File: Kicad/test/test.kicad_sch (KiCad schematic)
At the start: 72 parts, among them J1 SPKOUT, J2 PrgmUART, P1 USB_C_Plug_USB2.0, SW1 SW_Push, SW2 SW_Push, SW3 SW_Push, SW4 SW_Push, SW5 SW_Push, U1 MAX98357A, U2 ESP32-S3-WROOM-1

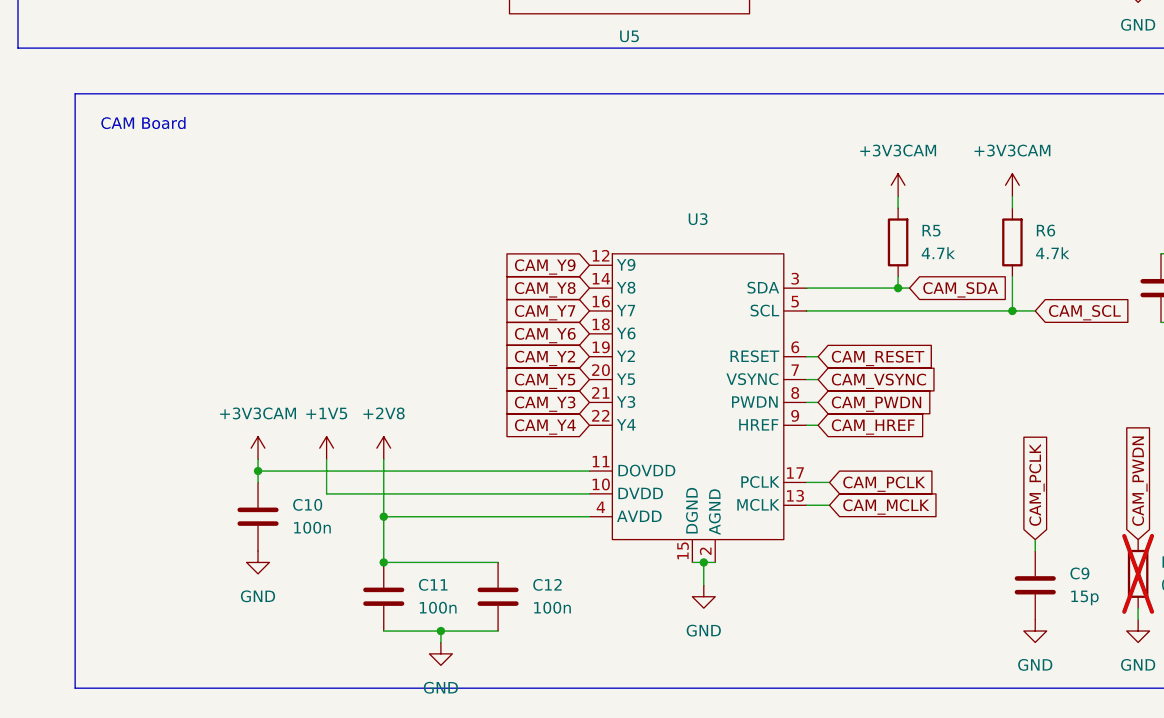
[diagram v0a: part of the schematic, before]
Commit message: Added Clock for Camera
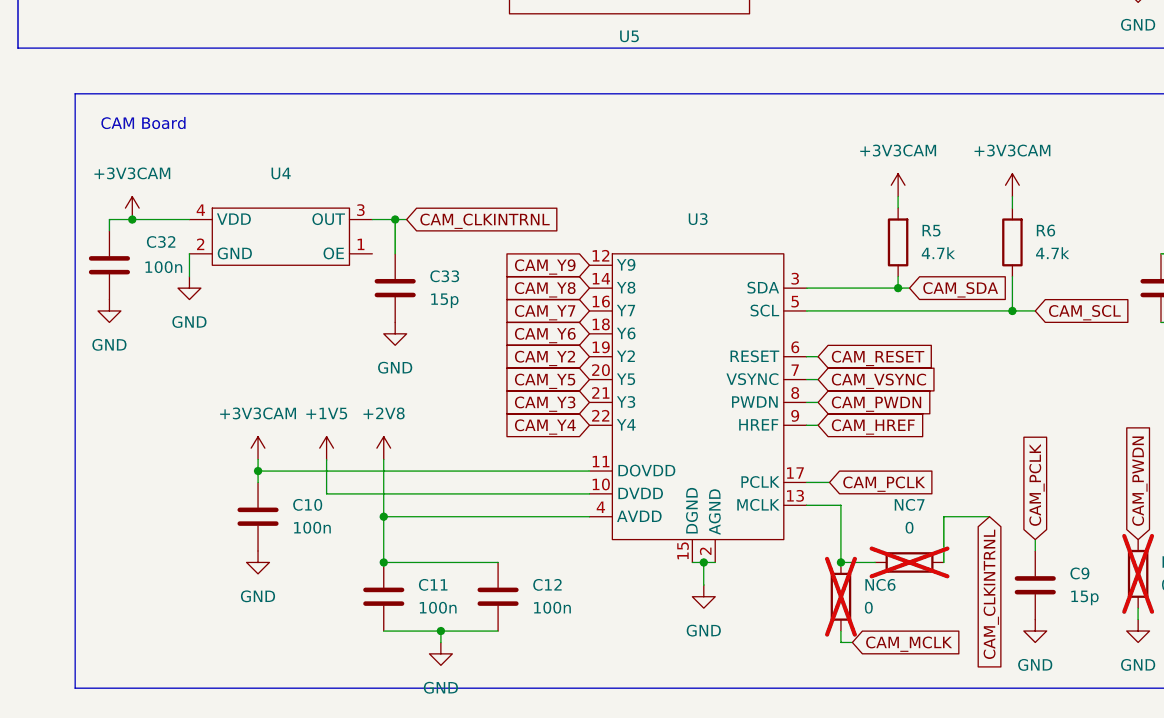
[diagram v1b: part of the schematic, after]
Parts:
- added C32: 100n, Capacitor_SMD:C_0603_1608Metric_Pad1.08x0.95mm_HandSolder, symbol Device:C
- added C33: 15p, Capacitor_SMD:C_0603_1608Metric_Pad1.08x0.95mm_HandSolder, symbol Device:C
- added NC6, NC7: 0, Resistor_SMD:R_1206_3216Metric, symbol Device:R
- added U4: ~, Footprint_Wareit_Mic:YSO110TR, symbol Components_Wareit_Mic:YSO110TR
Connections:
- net +3V3CAM: now also C32.1, U4.4 (VDD)
- net CAM_MCLK: now also NC6.2; no longer U3.13 (MCLK)
- net GND: now also C32.2, C33.2, U4.2 (GND)
- new net: NC6.1, NC7.2, U3.13 (MCLK)
- new net CAM_CLKINTRNL: C33.1, NC7.1, U4.3 (OUT)

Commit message: 3d Model Casing and PCB Added
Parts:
- removed D2: WS2812B, LED_SMD:LED_WS2812B_PLCC4_5.0x5.0mm_P3.2mm, symbol LED:WS2812B
- D4: LCSC Part (none) -> C22461793; Mfr Part (none) -> XL-5050RGBC-WS2812B-S
- L1, L2: footprint Capacitor_SMD:C_0603_1608Metric_Pad1.08x0.95mm_HandSolder -> Inductor_SMD:L_0805_2012Metric_Pad1.05x1.20mm_HandSolder; LCSC Part (none) -> C6364721; Mfr Part (none) -> AHW2012F-1R0KTF
- MK2: LCSC Part (none) -> C5656610; Mfr Part (none) -> ICS-43434
- P1: LCSC Part (none) -> C223907; Mfr Part (none) -> TYPE-C-31-M-14
- SW2, SW3, SW4: LCSC Part (none) -> C136662; Mfr Part (none) -> K2-1114SA-A4SW-06
- SW5: LCSC Part (none) -> C2733655; Mfr Part (none) -> B3S-1000
- U1: LCSC Part (none) -> C2682619; Mfr Part (none) -> MAX98357AEWL+T
- U3: value ~ -> OV5640; LCSC Part (none) -> C262669; Mfr Part (none) -> AFC01-S24FCA-00
- U4: value ~ -> 24Mhz; LCSC Part (none) -> C669072; Mfr Part (none) -> OT252024MJBA4SL
- U5: value ~ -> AXP2101; LCSC Part (none) -> C3036461; Mfr Part (none) -> AXP2101
- renumbered 3v3J to 3v3J1

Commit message: Floorplanning done
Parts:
- removed SW1: SW_Push, Button_Switch_SMD:SW_SPST_B3S-1000, symbol Switch:SW_Push
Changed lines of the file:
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@@
 	(wire
 		(pts
-			(xy 278.13 198.12) (xy 276.86 198.12)
-		)
-		(stroke
-			(width 0)
-			(type default)
-		)
-	)
-	(wire
-		(pts
 			(xy 214.63 96.52) (xy 222.25 96.52)
 		)
@@
 	(wire
 		(pts
-			(xy 276.86 198.12) (xy 276.86 201.93)
-		)
-		(stroke
-			(width 0)
-			(type default)
-		)
-	)
-	(wire
-		(pts
 			(xy 154.94 172.72) (xy 154.94 171.45)
 		)
@@
 		)
 	)
-	(global_label "EN"
-		(shape input)
-		(at 288.29 198.12 0)
-		(fields_autoplaced yes)
-		(effects
-			(font
-				(size 1.27 1.27)
-			)
-			(justify left)
-		)
-		(property "Intersheetrefs" "${INTERSHEET_REFS}"
-			(at 293.7547 198.12 0)
-			(effects
-				(font
-					(size 1.27 1.27)
-				)
-				(justify left)
-				(hide yes)
-			)
-		)
-	)
 	(global_label "CAM_MCLK"
 		(shape input)
@@
 	)
 	(symbol
-		(lib_id "power:GND")
-		(at 276.86 201.93 0)
-		(unit 1)
-		(exclude_from_sim no)
-		(in_bom yes)
-		(on_board yes)
-		(dnp no)
-		(property "Reference" "#PWR027"
-			(at 276.86 208.28 0)
-			(effects
-				(font
-					(size 1.27 1.27)
-				)
-				(hide yes)
-			)
-		)
-		(property "Value" "GND"
-			(at 276.86 207.01 0)
-			(effects
-				(font
-					(size 1.27 1.27)
-				)
-			)
-		)
-		(property "Footprint" ""
-			(at 276.86 201.93 0)
-			(effects
-				(font
-					(size 1.27 1.27)
-				)
-				(hide yes)
-			)
-		)
-		(property "Datasheet" ""
-			(at 276.86 201.93 0)
-			(effects
-				(font
-					(size 1.27 1.27)
-				)
-				(hide yes)
-			)
-		)
-		(property "Description" "Power symbol creates a global label with name \"GND\" , ground"
-			(at 276.86 201.93 0)
-			(effects
-				(font
-					(size 1.27 1.27)
-				)
-				(hide yes)
-			)
-		)
-		(pin "1"
-		)
-		(instances
-			(project "test"
-				(path "/2b9d0de6-8b12-4765-99af-867ac9f145de"
-					(reference "#PWR027")
-					(unit 1)
-				)
-			)
-		)
-	)
-	(symbol
 		(lib_id "Device:C")
 		(at 198.12 133.35 180)
@@
 					(unit 1)
 				)
-			)
-		)
-	)
-	(symbol
-		(lib_id "Switch:SW_Push")
-		(at 283.21 198.12 0)
-		(unit 1)
-		(exclude_from_sim no)
-		(in_bom yes)
-		(on_board yes)
-		(dnp no)
-		(fields_autoplaced yes)
-		(property "Reference" "SW1"
-			(at 283.21 190.5 0)
-			(effects
-				(font
-					(size 1.27 1.27)
-				)
-			)
-		)
-		(property "Value" "SW_Push"
-			(at 283.21 193.04 0)
-			(effects
-				(font
-					(size 1.27 1.27)
-				)
-			)
-		)
-		(property "Footprint" "Button_Switch_SMD:SW_SPST_B3S-1000"
-			(at 283.21 193.04 0)
-			(effects
-				(font
-					(size 1.27 1.27)
-				)
-				(hide yes)
-			)
-		)
-		(property "Datasheet" "~"
-			(at 283.21 193.04 0)
-			(effects
-				(font
-					(size 1.27 1.27)
-				)
-				(hide yes)
-			)
-		)
-		(property "Description" "Push button switch, generic, two pins"
-			(at 283.21 198.12 0)
-			(effects
-				(font
-					(size 1.27 1.27)
-				)
-				(hide yes)
-			)
-		)
-		(pin "1"
-		)
-		(pin "2"
-		)
-		(instances
-			(project ""
-				(path "/2b9d0de6-8b12-4765-99af-867ac9f145de"
-					(reference "SW1")
-					(unit 1)
-				)

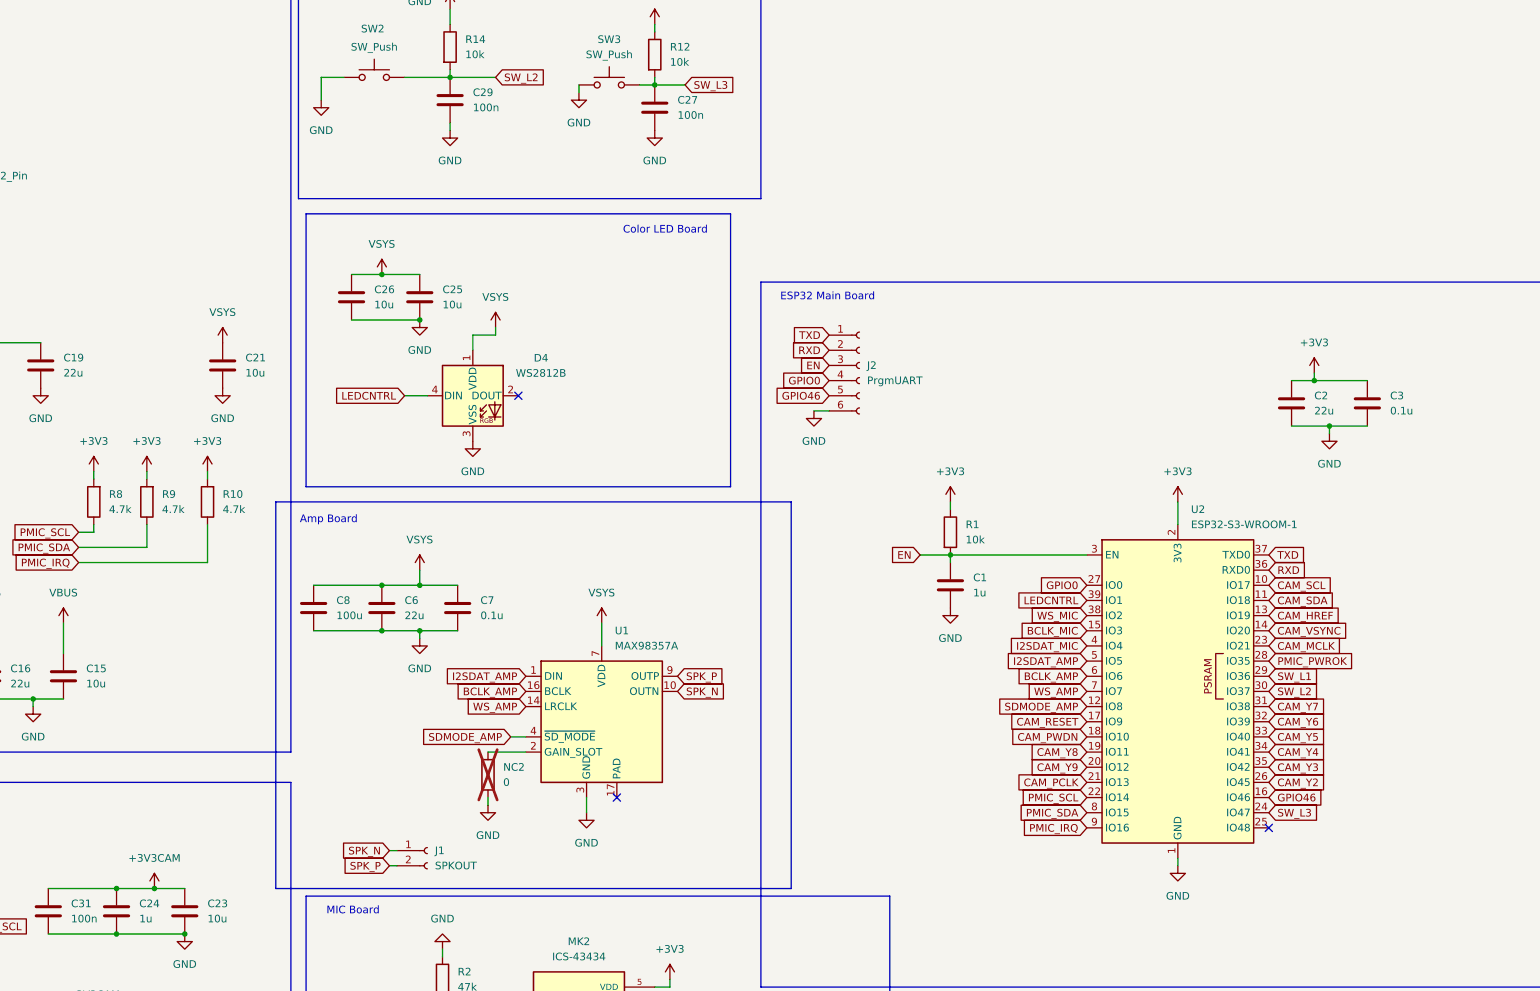
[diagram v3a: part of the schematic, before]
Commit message: Started PCB routing
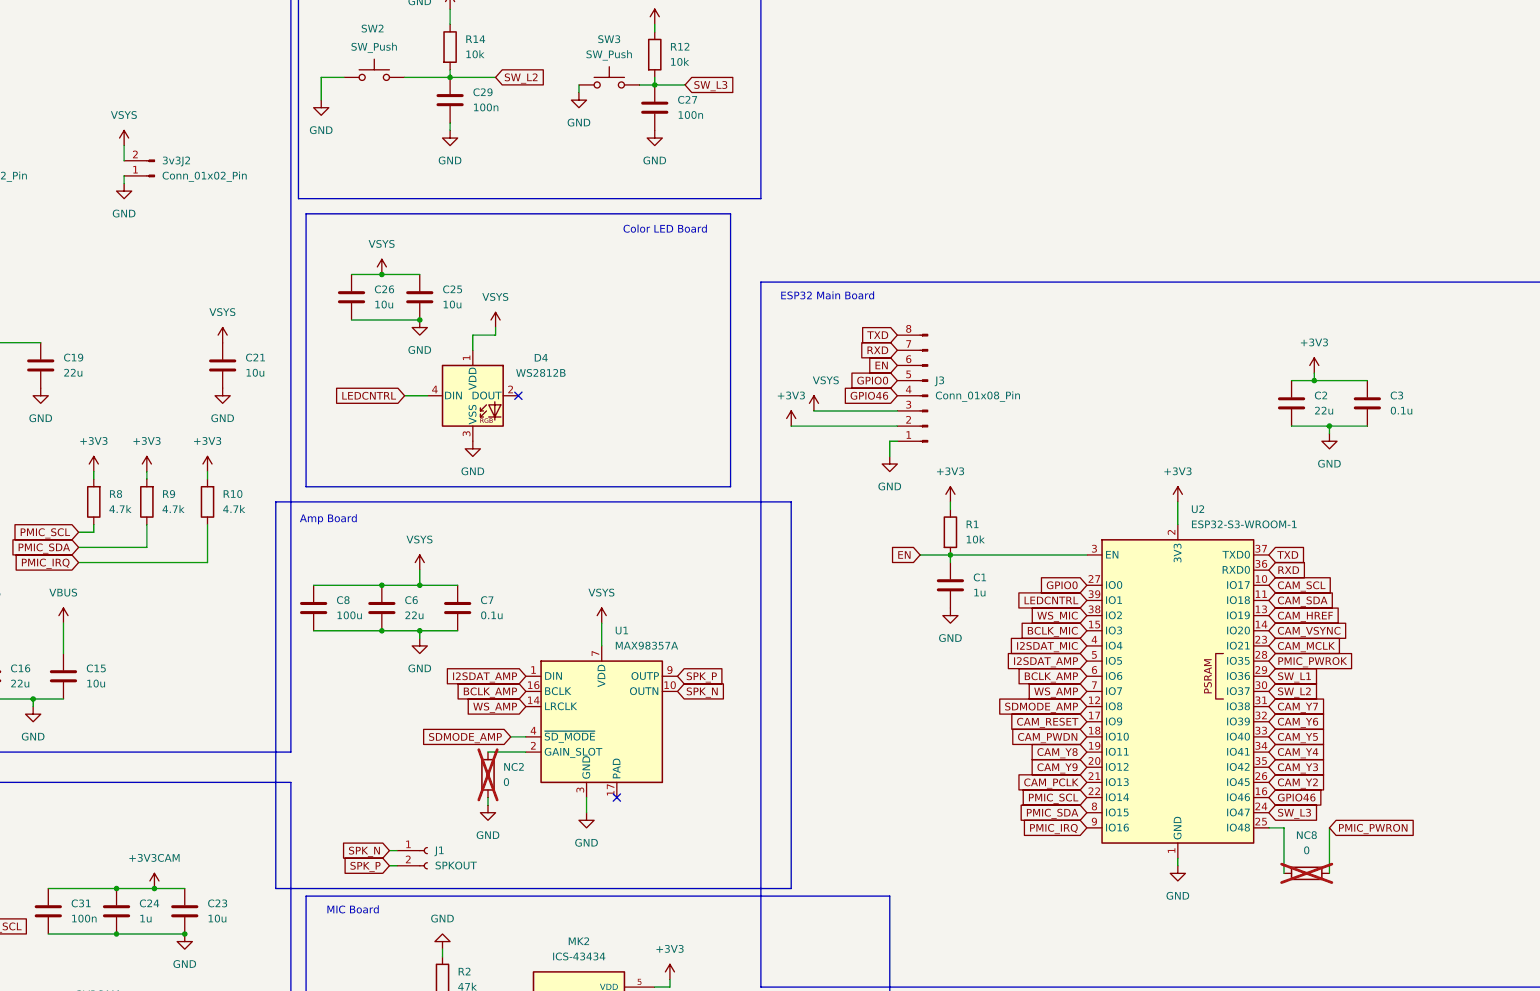
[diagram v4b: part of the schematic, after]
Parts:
- removed J2: PrgmUART, Connector_PinHeader_2.54mm:PinHeader_2x03_P2.54mm_Vertical, symbol Connector:Conn_01x06_Socket
- added 3v3J2: Conn_01x02_Pin, Footprint_Wareit_Mic:SMD_CONNECTOR_PAD, symbol Connector:Conn_01x02_Pin
- added J3: Conn_01x08_Pin, Connector_PinHeader_2.54mm:PinHeader_2x04_P2.54mm_Vertical, symbol Connector:Conn_01x08_Pin
- added NC8: 0, Resistor_SMD:R_1206_3216Metric, symbol Device:R
- 3v3J1, BAT1, J1: footprint Connector_PinHeader_2.54mm:PinHeader_1x02_P2.54mm_Vertical -> Footprint_Wareit_Mic:SMD_CONNECTOR_PAD
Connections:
- net +3V3: now also J3.2 (Pin_2)
- net EN: now also J3.6 (Pin_6)
- net GND: now also 3v3J2.1 (Pin_1), J3.1 (Pin_1)
- net GPIO0: now also J3.5 (Pin_5)
- net GPIO46: now also J3.4 (Pin_4)
- net PMIC_PWRON: now also NC8.2
- net RXD: now also J3.7 (Pin_7)
- net TXD: now also J3.8 (Pin_8)
- net VSYS: now also 3v3J2.2 (Pin_2), J3.3 (Pin_3)
- net at U2.25 (IO48): now also NC8.1
- no-connect marks 26 -> 25

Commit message: Updated schematics
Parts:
- R5, R6, R8, R9: value 4.7k -> 10k
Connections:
- net PMIC_SCL is gone; now on net CAM_SCL: R8.1, U2.22 (IO14), U5.40 (SCK)
- net PMIC_SDA is gone; now on net CAM_SDA: R9.1, U2.8 (IO15), U5.39 (SDA)
- net CAM_SCL: no longer U2.10 (IO17)
- net CAM_SDA: no longer U2.11 (IO18)
- net SW_L1: now also U2.10 (IO17); no longer U2.29 (IO36)
- net SW_L2: now also U2.11 (IO18); no longer U2.30 (IO37)
- net PMIC_PWROK: no longer names the net of U5.29 (PWROK)
- net PMIC_PWROK: no longer U2.28 (IO35)
- no-connect marks 25 -> 29
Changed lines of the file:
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@@
 	)
 	(no_connect
+		(at 351.79 194.31)
+	)
+	(no_connect
 		(at 104.14 160.02)
 	)
@@
 	)
 	(no_connect
+		(at 351.79 196.85)
+	)
+	(no_connect
 		(at 104.14 186.69)
 	)
@@
 	)
 	(no_connect
+		(at 72.39 143.51)
+	)
+	(no_connect
 		(at 104.14 167.64)
 	)
@@
 	)
 	(no_connect
+		(at 351.79 199.39)
+	)
+	(no_connect
 		(at 60.96 86.36)
 	)
@@
 	(wire
 		(pts
+			(xy 378.46 170.18) (xy 382.27 170.18)
+		)
+		(stroke
+			(width 0)
+			(type default)
+		)
+	)
+	(wire
+		(pts
+			(xy 378.46 167.64) (xy 382.27 167.64)
+		)
+		(stroke
+			(width 0)
+			(type default)
+		)
+	)
+	(wire
+		(pts
 			(xy 165.1 232.41) (xy 170.18 232.41)
 		)
@@
 	(wire
 		(pts
-			(xy 72.39 143.51) (xy 71.12 143.51)
-		)
-		(stroke
-			(width 0)
-			(type default)
-		)
-	)
-	(wire
-		(pts
 			(xy 123.19 266.7) (xy 123.19 261.62)
 		)
@@
 	(global_label "CAM_SDA"
 		(shape input)
-		(at 351.79 184.15 0)
+		(at 382.27 170.18 0)
 		(fields_autoplaced yes)
 		(effects
@@
 		)
 		(property "Intersheetrefs" "${INTERSHEET_REFS}"
-			(at 363.1209 184.15 0)
+			(at 393.6009 170.18 0)
 			(effects
 				(font
@@
 		)
 	)
-	(global_label "GPIO46"
+	(global_label "SW_L2"
 		(shape input)
-		(at 351.79 217.17 0)
+		(at 351.79 184.15 0)
 		(fields_autoplaced yes)
 		(effects
@@
 		)
 		(property "Intersheetrefs" "${INTERSHEET_REFS}"
-			(at 361.6695 217.17 0)
+			(at 360.6413 184.15 0)
 			(effects
 				(font
@@
 		)
 	)
-	(global_label "BCLK_AMP"
+	(global_label "GPIO46"
 		(shape input)
-		(at 321.31 196.85 180)
+		(at 351.79 217.17 0)
 		(fields_autoplaced yes)
 		(effects
@@
 				(size 1.27 1.27)
 			)
-			(justify right)
+			(justify left)
 		)
 		(property "Intersheetrefs" "${INTERSHEET_REFS}"
-			(at 308.7091 196.85 0)
+			(at 361.6695 217.17 0)
 			(effects
 				(font
 					(size 1.27 1.27)
 				)
-				(justify right)
+				(justify left)
 				(hide yes)
 			)
 		)
 	)
-	(global_label "WS_MIC"
+	(global_label "BCLK_AMP"
 		(shape input)
-		(at 321.31 186.69 180)
+		(at 321.31 196.85 180)
 		(fields_autoplaced yes)
 		(effects
@@
 		)
 		(property "Intersheetrefs" "${INTERSHEET_REFS}"
-			(at 311.3701 186.69 0)
+			(at 308.7091 196.85 0)
 			(effects
 				(font
@@
 		)
 	)
-	(global_label "SW_L2"
+	(global_label "WS_MIC"
 		(shape input)
-		(at 351.79 199.39 0)
+		(at 321.31 186.69 180)
 		(fields_autoplaced yes)
 		(effects
@@
 				(size 1.27 1.27)
 			)
-			(justify left)
+			(justify right)
 		)
 		(property "Intersheetrefs" "${INTERSHEET_REFS}"
-			(at 360.6413 199.39 0)
+			(at 311.3701 186.69 0)
 			(effects
 				(font
 					(size 1.27 1.27)
 				)
-				(justify left)
+				(justify right)
 				(hide yes)
 			)
@@
 		)
 	)
-	(global_label "SW_L1"
-		(shape input)
-		(at 351.79 196.85 0)
-		(fields_autoplaced yes)
-		(effects
-			(font
-				(size 1.27 1.27)
-			)
-			(justify left)
-		)
-		(property "Intersheetrefs" "${INTERSHEET_REFS}"
-			(at 360.6413 196.85 0)
-			(effects
-				(font
-					(size 1.27 1.27)
-				)
-				(justify left)
-				(hide yes)
-			)
-		)
-	)
 	(global_label "CAM_SCL"
 		(shape input)
@@
 		)
 	)
+	(global_label "PMIC_SCL"
+		(shape input)
+		(at 378.46 167.64 180)
+		(fields_autoplaced yes)
+		(effects
+			(font
+				(size 1.27 1.27)
+			)
+			(justify right)
+		)
+		(property "Intersheetrefs" "${INTERSHEET_REFS}"
+			(at 366.4034 167.64 0)
+			(effects
+				(font
+					(size 1.27 1.27)
+				)
+				(justify right)
+				(hide yes)
+			)
+		)
+	)
+	(global_label "SW_L1"
+		(shape input)
+		(at 351.79 181.61 0)
+		(fields_autoplaced yes)
+		(effects
+			(font
+				(size 1.27 1.27)
+			)
+			(justify left)
+		)
+		(property "Intersheetrefs" "${INTERSHEET_REFS}"
+			(at 360.6413 181.61 0)
+			(effects
+				(font
+					(size 1.27 1.27)
+				)
+				(justify left)
+				(hide yes)
+			)
+		)
+	)
 	(global_label "CAM_PWDN"
 		(shape input)
@@
 		)
 	)
-	(global_label "PMIC_PWROK"
-		(shape input)
-		(at 71.12 143.51 180)
-		(fields_autoplaced yes)
-		(effects
-			(font
-				(size 1.27 1.27)
-			)
-			(justify right)
-		)
-		(property "Intersheetrefs" "${INTERSHEET_REFS}"
-			(at 55.9791 143.51 0)
-			(effects
-				(font
-					(size 1.27 1.27)
-				)
-				(justify right)
-				(hide yes)
-			)
-		)
-	)
 	(global_label "CAM_RESET"
 		(shape input)
@@
 		)
 	)
+	(global_label "PMIC_SDA"
+		(shape input)
+		(at 378.46 170.18 180)
+		(fields_autoplaced yes)
+		(effects
+			(font
+				(size 1.27 1.27)
+			)
+			(justify right)
+		)
+		(property "Intersheetrefs" "${INTERSHEET_REFS}"
+			(at 366.3429 170.18 0)
+			(effects
+				(font
+					(size 1.27 1.27)
+				)
+				(justify right)
+				(hide yes)
+			)
+		)
+	)
 	(global_label "PMIC_SCL"
 		(shape input)
@@
 	(global_label "CAM_SCL"
 		(shape input)
-		(at 351.79 181.61 0)
+		(at 382.27 167.64 0)
 		(fields_autoplaced yes)
 		(effects
@@
 		)
 		(property "Intersheetrefs" "${INTERSHEET_REFS}"
-			(at 363.0604 181.61 0)
+			(at 393.5404 167.64 0)
 			(effects
 				(font
@@
 		)
 	)
-	(global_label "PMIC_PWROK"
-		(shape input)
-		(at 351.79 194.31 0)
-		(fields_autoplaced yes)
-		(effects
-			(font
-				(size 1.27 1.27)
-			)
-			(justify left)
-		)
-		(property "Intersheetrefs" "${INTERSHEET_REFS}"
-			(at 366.9309 194.31 0)
-			(effects
-				(font
-					(size 1.27 1.27)
-				)
-				(justify left)
-				(hide yes)
-			)
-		)
-	)
 	(global_label "EN"
 		(shape input)
@@
 			)
 		)
-		(property "Value" "4.7k"
+		(property "Value" "10k"
 			(at 133.35 232.4099 0)
 			(effects
@@
 			)
 		)
-		(property "Value" "4.7k"
+		(property "Value" "10k"
 			(at 120.65 232.4099 0)
 			(effects
@@
 			)
 		)
-		(property "Value" "4.7k"
+		(property "Value" "10k"
 			(at 166.37 168.9099 0)
 			(effects
@@
 			)
 		)
-		(property "Value" "4.7k"
+		(property "Value" "10k"
 			(at 157.48 168.9099 0)
 			(effects
